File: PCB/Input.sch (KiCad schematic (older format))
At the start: 35 parts, among them SW1 PCB_Switch_Winkel_THT, SW2 PCB_Switch_Winkel_THT, SW3 PCB_Switch_Winkel_THT, SW4 PCB_Switch_Winkel_THT, SW5 PCB_Switch_Winkel_THT, SW6 Rotary_stehend_THT

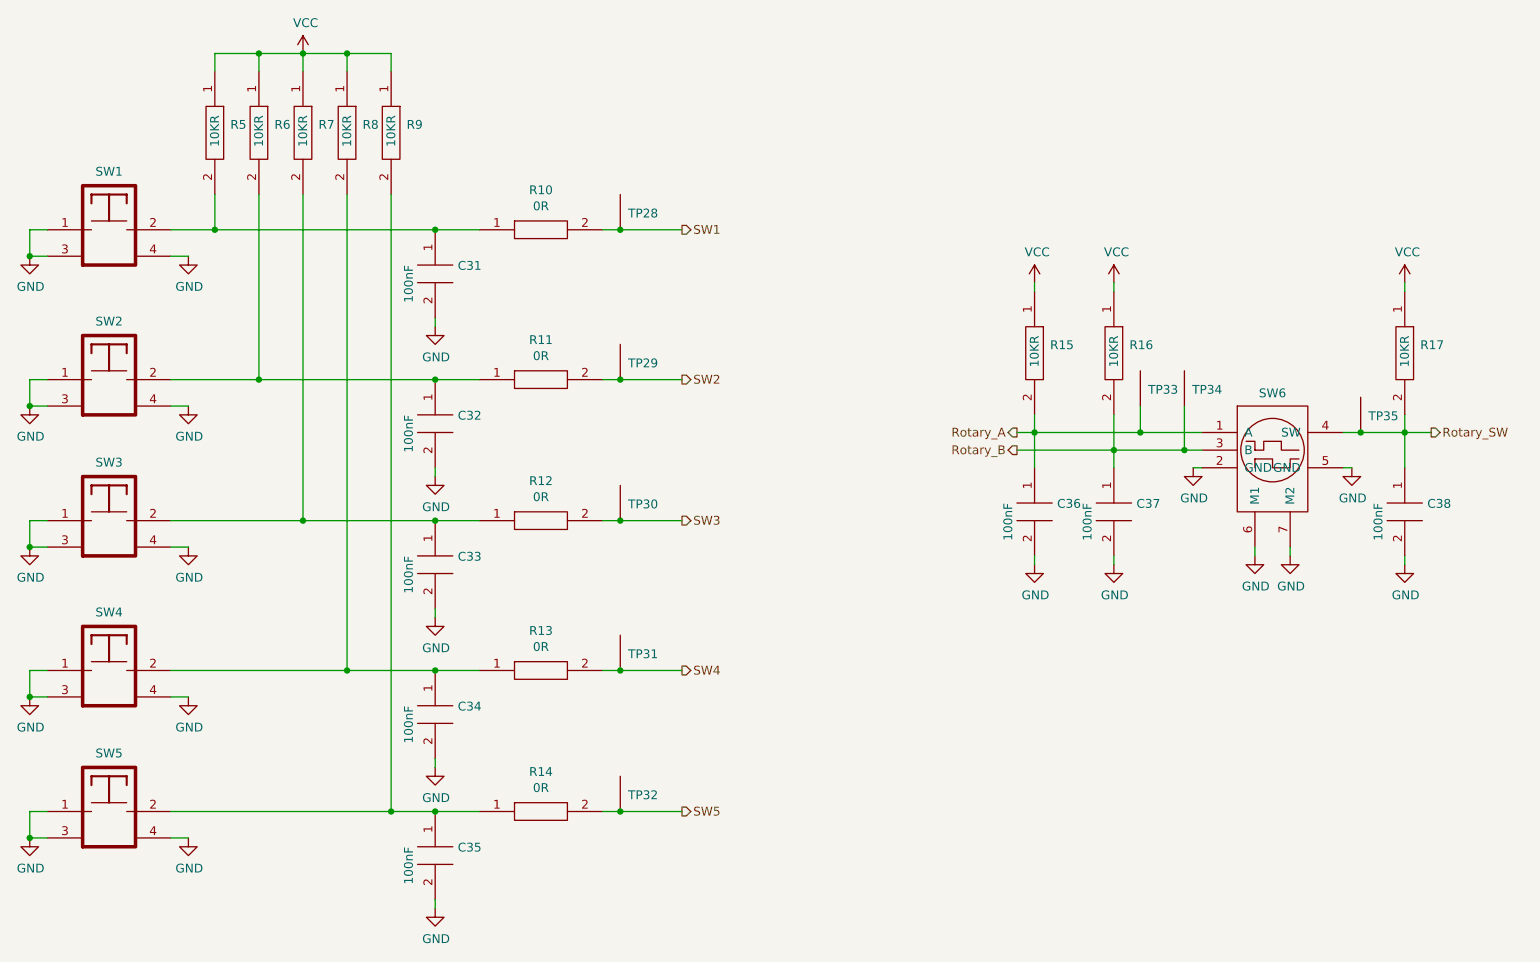
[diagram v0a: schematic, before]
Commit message: Sheet USB
USB Switch und USB Input Stecker hinzugefügt
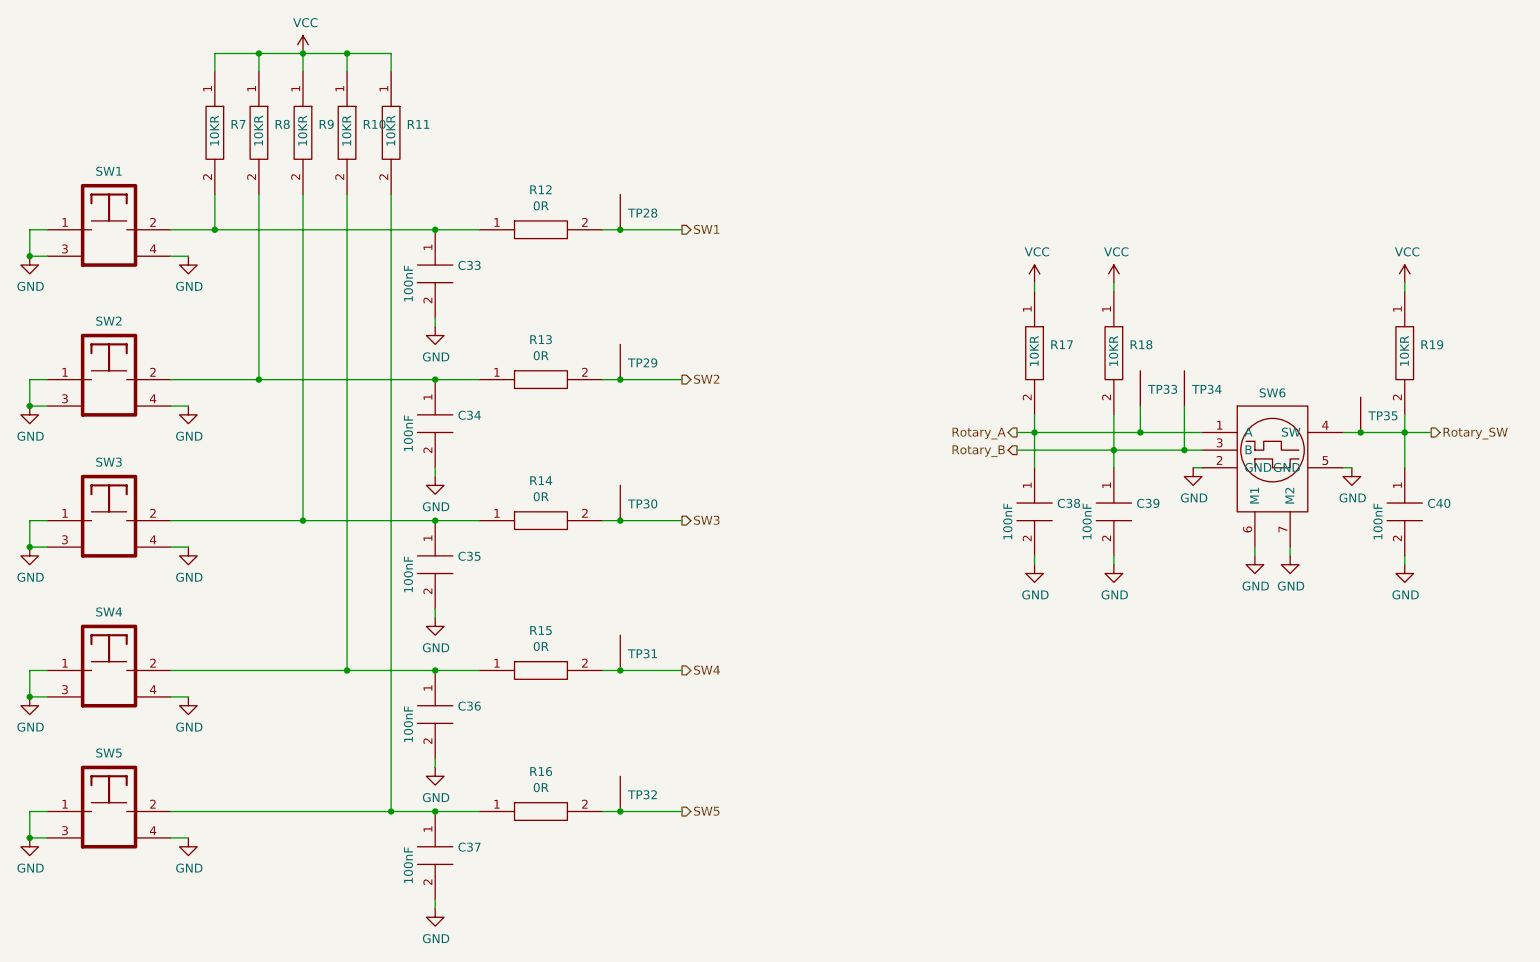
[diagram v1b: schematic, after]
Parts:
- renumbered C31 to C33, C32 to C34, C33 to C35, C34 to C36, C35 to C37, C36 to C38, C37 to C39, C38 to C40, R8 to R10, R9 to R11, R10 to R12, R11 to R13, R12 to R14, R13 to R15, R14 to R16, R15 to R17, R16 to R18, R17 to R19, R5 to R7, R6 to R8, R7 to R9
